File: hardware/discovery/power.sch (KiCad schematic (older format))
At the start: 9 parts, among them U2 MCP73831, U3 BD33IA5

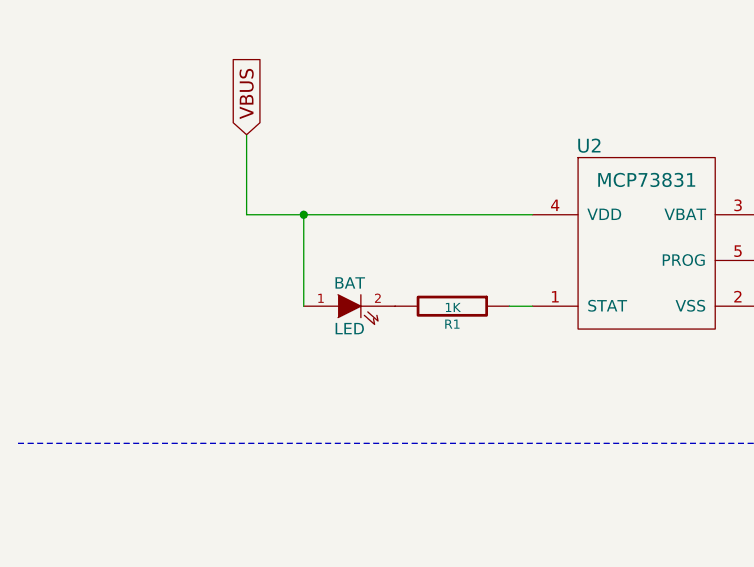
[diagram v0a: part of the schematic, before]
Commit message: Discovery: Fix channel button labels
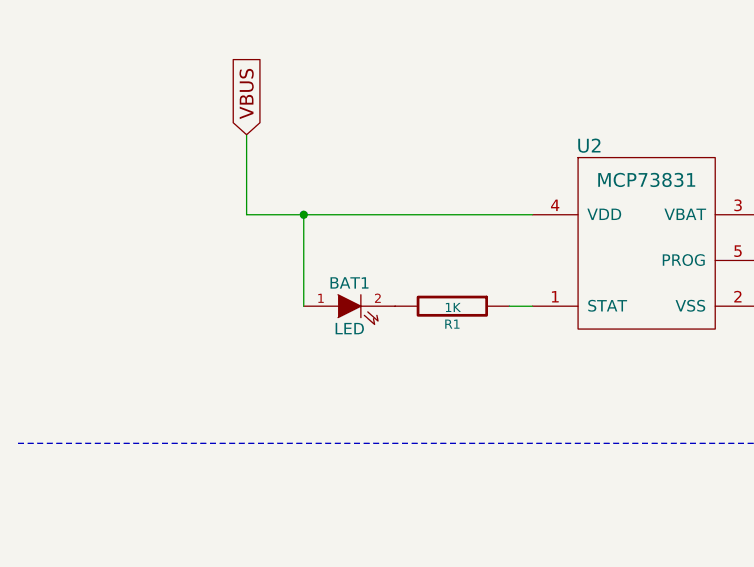
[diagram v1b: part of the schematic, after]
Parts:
- BAT1: renamed from BAT; footprint (none) -> Diodes_SMD:D_0805
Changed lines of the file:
@@
 $EndComp
 $Comp
-L GND #PWR02
+L GND #PWR07
 U 1 1 585D2F29
 P 4400 2900
-F 0 "#PWR02" H 4400 2900 30  0001 C CNN
+F 0 "#PWR07" H 4400 2900 30  0001 C CNN
 F 1 "GND" H 4400 2830 30  0001 C CNN
 F 2 "" H 4400 2900 60  0001 C CNN
@@
 	4700 2300 4700 1950
 $Comp
-L LED BAT
+L LED BAT1
 U 1 1 585D348C
 P 1950 2700
-F 0 "BAT" H 1950 2800 50  0000 C CNN
+F 0 "BAT1" H 1950 2800 50  0000 C CNN
 F 1 "LED" H 1950 2600 50  0000 C CNN
-F 2 "" H 1950 2700 60  0001 C CNN
+F 2 "Diodes_SMD:D_0805" H 1950 2700 60  0001 C CNN
 F 3 "" H 1950 2700 60  0000 C CNN
 	1    1950 2700
@@
 VBUS
 $Comp
-L PWR_FLAG #FLG03
+L PWR_FLAG #FLG08
 U 1 1 585D38B1
 P 4300 6300
-F 0 "#FLG03" H 4300 6395 30  0001 C CNN
+F 0 "#FLG08" H 4300 6395 30  0001 C CNN
 F 1 "PWR_FLAG" H 4300 6480 30  0000 C CNN
 F 2 "" H 4300 6300 60  0001 C CNN
@@
 $EndComp
 $Comp
-L PWR_FLAG #FLG04
+L PWR_FLAG #FLG09
 U 1 1 585D3922
 P 4300 6650
-F 0 "#FLG04" H 4300 6745 30  0001 C CNN
+F 0 "#FLG09" H 4300 6745 30  0001 C CNN
 F 1 "PWR_FLAG" H 4300 6830 30  0000 C CNN
 F 2 "" H 4300 6650 60  0001 C CNN
@@
 VIN
 $Comp
-L GND #PWR05
+L GND #PWR010
 U 1 1 585D49CE
 P 7750 2500
-F 0 "#PWR05" H 7750 2500 30  0001 C CNN
+F 0 "#PWR010" H 7750 2500 30  0001 C CNN
 F 1 "GND" H 7750 2430 30  0001 C CNN
 F 2 "" H 7750 2500 60  0001 C CNN
@@
 3V3
 $Comp
-L PWR_FLAG #FLG06
+L PWR_FLAG #FLG011
 U 1 1 585D561D
 P 4300 7000
-F 0 "#FLG06" H 4300 7095 30  0001 C CNN
+F 0 "#FLG011" H 4300 7095 30  0001 C CNN
 F 1 "PWR_FLAG" H 4300 7180 30  0000 C CNN
 F 2 "" H 4300 7000 60  0001 C CNN
@@
 $EndComp
 $Comp
-L GND #PWR07
+L GND #PWR012
 U 1 1 585D5C16
 P 9600 2300
-F 0 "#PWR07" H 9600 2300 30  0001 C CNN
+F 0 "#PWR012" H 9600 2300 30  0001 C CNN
 F 1 "GND" H 9600 2230 30  0001 C CNN
 F 2 "" H 9600 2300 60  0001 C CNN

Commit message: Discovery start power section
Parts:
- removed D27: DOUBLE_SCH_KCOM, TO_SOT_Packages_SMD:SOT-23_Handsoldering, symbol DOUBLE_SCH_KCOM
- added BT1: BATTERY, Connect:PINHEAD1-2, symbol BATTERY
- added CON1: USB-MICRO-B, Connect:USB_Micro-B, symbol USB-MICRO-B
- added D27: DOUBLE_SCH_KCOM_PMEG2005CT, TO_SOT_Packages_SMD:SOT-23, symbol DOUBLE_SCH_KCOM_PMEG2005CT
- C1, C2: footprint (none) -> Capacitors_SMD:C_0805
- C3: footprint (none) -> Capacitors_SMD:C_1206
- R1, R2: footprint (none) -> Resistors_SMD:R_0805
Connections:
- net labels added: FS_DM, FS_DP
- wire segments 19 -> 26
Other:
- note added: "R2 = 10K => 100mA charge\n"
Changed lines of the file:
@@
 LIBS:contrib
 LIBS:valves
-LIBS:w_connectors
 LIBS:stm32f4_disco_header
 LIBS:74xgxx
@@
 F 0 "R2" V 4130 2500 40  0000 C CNN
 F 1 "10K" V 4057 2501 40  0000 C CNN
-F 2 "" V 3980 2500 30  0001 C CNN
+F 2 "Resistors_SMD:R_0805" V 3980 2500 30  0001 C CNN
 F 3 "" H 4050 2500 30  0000 C CNN
 	1    4050 2500
@@
 F 0 "C1" H 4700 2600 40  0000 L CNN
 F 1 "10uF" H 4706 2415 40  0000 L CNN
-F 2 "" H 4738 2350 30  0001 C CNN
+F 2 "Capacitors_SMD:C_0805" H 4738 2350 30  0001 C CNN
 F 3 "" H 4700 2500 60  0000 C CNN
 	1    4700 2500
@@
 F 0 "R1" V 2480 2700 40  0000 C CNN
 F 1 "1K" V 2407 2701 40  0000 C CNN
-F 2 "" V 2330 2700 30  0001 C CNN
+F 2 "Resistors_SMD:R_0805" V 2330 2700 30  0001 C CNN
 F 3 "" H 2400 2700 30  0000 C CNN
 	1    2400 2700
@@
 	1    0    0    -1
 $EndComp
-$Comp
-L DOUBLE_SCH_KCOM D27
-U 1 1 585D4394
-P 5550 6750
-F 0 "D27" H 5700 6625 60  0000 C CNN
-F 1 "DOUBLE_SCH_KCOM" H 5550 6900 60  0000 C CNN
-F 2 "TO_SOT_Packages_SMD:SOT-23_Handsoldering" H 5550 6750 60  0001 C CNN
-F 3 "" H 5550 6750 60  0000 C CNN
-	1    5550 6750
-	-1   0    0    1
-$EndComp
-Text GLabel 5150 6750 0    60   Input ~ 0
+Text GLabel 5950 6750 2    60   Input ~ 0
 VBUS
 Text GLabel 5550 6550 1    60   Input ~ 0
 VIN
-Text GLabel 5950 6750 2    60   Input ~ 0
+Text GLabel 5150 6750 0    60   Input ~ 0
 VBAT
 Wire Wire Line
@@
 F 0 "C3" H 9600 2200 40  0000 L CNN
 F 1 "47uF" H 9606 2015 40  0000 L CNN
-F 2 "" H 9638 1950 30  0001 C CNN
+F 2 "Capacitors_SMD:C_1206" H 9638 1950 30  0001 C CNN
 F 3 "" H 9600 2100 60  0000 C CNN
 	1    9600 2100
@@
 F 0 "C2" H 7750 2200 40  0000 L CNN
 F 1 "4.7uF" H 7756 2015 40  0000 L CNN
-F 2 "" H 7788 1950 30  0001 C CNN
+F 2 "Capacitors_SMD:C_0805" H 7788 1950 30  0001 C CNN
 F 3 "" H 7750 2100 60  0000 C CNN
 	1    7750 2100
@@
 Wire Wire Line
 	3800 2500 3750 2500
+$Comp
+L USB-MICRO-B CON1
+U 1 1 585CF6A2
+P 4450 4500
+F 0 "CON1" H 4200 4950 60  0000 C CNN
+F 1 "USB-MICRO-B" H 4400 4000 60  0000 C CNN
+F 2 "Connect:USB_Micro-B" H 4450 4500 60  0001 C CNN
+F 3 "" H 4450 4500 60  0001 C CNN
+	1    4450 4500
+	1    0    0    -1
+$EndComp
+Wire Wire Line
+	5000 4200 5200 4200
+Wire Wire Line
+	5200 4200 5200 5000
+Wire Wire Line
+	5000 4350 5200 4350
+Connection ~ 5200 4350
+Wire Wire Line
+	5000 4650 5200 4650
+Connection ~ 5200 4650
+Wire Wire Line
+	5000 4800 5200 4800
+Connection ~ 5200 4800
+$Comp
+L GND #PWR013
+U 1 1 585CFC1E
+P 5200 5000
+F 0 "#PWR013" H 5200 5000 30  0001 C CNN
+F 1 "GND" H 5200 4930 30  0001 C CNN
+F 2 "" H 5200 5000 60  0001 C CNN
+F 3 "" H 5200 5000 60  0001 C CNN
+	1    5200 5000
+	1    0    0    -1
+$EndComp
+Text GLabel 3900 4200 0    60   Input ~ 0
+VBUS
+Wire Wire Line
+	3900 4800 3700 4800
+Wire Wire Line
+	3700 4800 3700 5000
+$Comp
+L GND #PWR014
+U 1 1 585CFC9F
+P 3700 5000
+F 0 "#PWR014" H 3700 5000 30  0001 C CNN
+F 1 "GND" H 3700 4930 30  0001 C CNN
+F 2 "" H 3700 5000 60  0001 C CNN
+F 3 "" H 3700 5000 60  0001 C CNN
+	1    3700 5000
+	1    0    0    -1
+$EndComp
+Text Notes 3800 3100 0    60   ~ 0
+R2 = 10K => 100mA charge\n
+$Comp
+L DOUBLE_SCH_KCOM_PMEG2005CT D27
+U 1 1 585D07BB
+P 5550 6750
+F 0 "D27" H 5700 6625 60  0000 C CNN
+F 1 "DOUBLE_SCH_KCOM_PMEG2005CT" H 5550 6900 60  0000 C CNN
+F 2 "TO_SOT_Packages_SMD:SOT-23" H 5550 6750 60  0001 C CNN
+F 3 "" H 5550 6750 60  0000 C CNN
+	1    5550 6750
+	-1   0    0    1
+$EndComp
+Text GLabel 3900 4350 0    60   Input ~ 0
+FS_DM
+Text GLabel 3900 4500 0    60   Input ~ 0
+FS_DP
+$Comp
+L BATTERY BT1
+U 1 1 585D1A2B
+P 2150 4500
+F 0 "BT1" H 2150 4700 50  0000 C CNN
+F 1 "BATTERY" H 2150 4310 50  0000 C CNN
+F 2 "Connect:PINHEAD1-2" H 2150 4500 60  0001 C CNN
+F 3 "" H 2150 4500 60  0000 C CNN
+	1    2150 4500
+	0    1    1    0
+$EndComp
+Text GLabel 2150 4200 1    60   Input ~ 0
+VBAT
+$Comp
+L GND #PWR015
+U 1 1 585D1BAC
+P 2150 4800
+F 0 "#PWR015" H 2150 4800 30  0001 C CNN
+F 1 "GND" H 2150 4730 30  0001 C CNN
+F 2 "" H 2150 4800 60  0001 C CNN
+F 3 "" H 2150 4800 60  0001 C CNN
+	1    2150 4800
+	1    0    0    -1
+$EndComp
 $EndSCHEMATC

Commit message: Discovery: Connect all button to the wakeup pin
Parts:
- BAT1: footprint Diodes_SMD:D_0805 -> LEDs:LED_0805
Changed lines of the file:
@@
 $EndComp
 $Comp
-L GND #PWR07
+L GND #PWR04
 U 1 1 585D2F29
 P 4400 2900
-F 0 "#PWR07" H 4400 2900 30  0001 C CNN
+F 0 "#PWR04" H 4400 2900 30  0001 C CNN
 F 1 "GND" H 4400 2830 30  0001 C CNN
 F 2 "" H 4400 2900 60  0001 C CNN
@@
 F 0 "BAT1" H 1950 2800 50  0000 C CNN
 F 1 "LED" H 1950 2600 50  0000 C CNN
-F 2 "Diodes_SMD:D_0805" H 1950 2700 60  0001 C CNN
+F 2 "LEDs:LED_0805" H 1950 2700 60  0001 C CNN
 F 3 "" H 1950 2700 60  0000 C CNN
 	1    1950 2700
@@
 VBUS
 $Comp
-L PWR_FLAG #FLG08
+L PWR_FLAG #FLG05
 U 1 1 585D38B1
 P 4300 6300
-F 0 "#FLG08" H 4300 6395 30  0001 C CNN
+F 0 "#FLG05" H 4300 6395 30  0001 C CNN
 F 1 "PWR_FLAG" H 4300 6480 30  0000 C CNN
 F 2 "" H 4300 6300 60  0001 C CNN
@@
 $EndComp
 $Comp
-L PWR_FLAG #FLG09
+L PWR_FLAG #FLG06
 U 1 1 585D3922
 P 4300 6650
-F 0 "#FLG09" H 4300 6745 30  0001 C CNN
+F 0 "#FLG06" H 4300 6745 30  0001 C CNN
 F 1 "PWR_FLAG" H 4300 6830 30  0000 C CNN
 F 2 "" H 4300 6650 60  0001 C CNN
@@
 VIN
 $Comp
-L GND #PWR010
+L GND #PWR07
 U 1 1 585D49CE
 P 7750 2500
-F 0 "#PWR010" H 7750 2500 30  0001 C CNN
+F 0 "#PWR07" H 7750 2500 30  0001 C CNN
 F 1 "GND" H 7750 2430 30  0001 C CNN
 F 2 "" H 7750 2500 60  0001 C CNN
@@
 3V3
 $Comp
-L PWR_FLAG #FLG011
+L PWR_FLAG #FLG08
 U 1 1 585D561D
 P 4300 7000
-F 0 "#FLG011" H 4300 7095 30  0001 C CNN
+F 0 "#FLG08" H 4300 7095 30  0001 C CNN
 F 1 "PWR_FLAG" H 4300 7180 30  0000 C CNN
 F 2 "" H 4300 7000 60  0001 C CNN
@@
 $EndComp
 $Comp
-L GND #PWR012
+L GND #PWR09
 U 1 1 585D5C16
 P 9600 2300
-F 0 "#PWR012" H 9600 2300 30  0001 C CNN
+F 0 "#PWR09" H 9600 2300 30  0001 C CNN
 F 1 "GND" H 9600 2230 30  0001 C CNN
 F 2 "" H 9600 2300 60  0001 C CNN
@@
 Connection ~ 5200 4800
 $Comp
-L GND #PWR013
+L GND #PWR010
 U 1 1 585CFC1E
 P 5200 5000
-F 0 "#PWR013" H 5200 5000 30  0001 C CNN
+F 0 "#PWR010" H 5200 5000 30  0001 C CNN
 F 1 "GND" H 5200 4930 30  0001 C CNN
 F 2 "" H 5200 5000 60  0001 C CNN
@@
 	3700 4800 3700 5000
 $Comp
-L GND #PWR014
+L GND #PWR011
 U 1 1 585CFC9F
 P 3700 5000
-F 0 "#PWR014" H 3700 5000 30  0001 C CNN
+F 0 "#PWR011" H 3700 5000 30  0001 C CNN
 F 1 "GND" H 3700 4930 30  0001 C CNN
 F 2 "" H 3700 5000 60  0001 C CNN
@@
 VBAT
 $Comp
-L GND #PWR015
+L GND #PWR012
 U 1 1 585D1BAC
 P 2150 4800
-F 0 "#PWR015" H 2150 4800 30  0001 C CNN
+F 0 "#PWR012" H 2150 4800 30  0001 C CNN
 F 1 "GND" H 2150 4730 30  0001 C CNN
 F 2 "" H 2150 4800 60  0001 C CNN

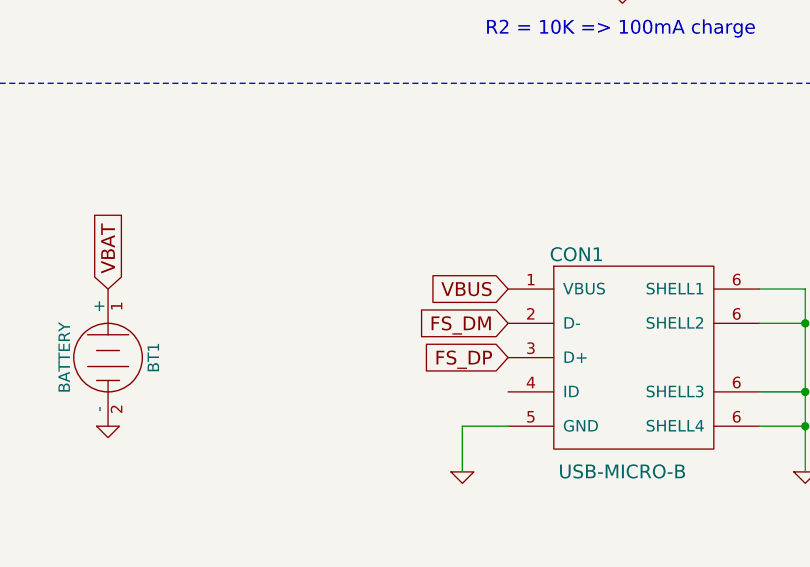
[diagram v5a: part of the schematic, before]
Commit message: Discovery: STM32F4 power a filtering
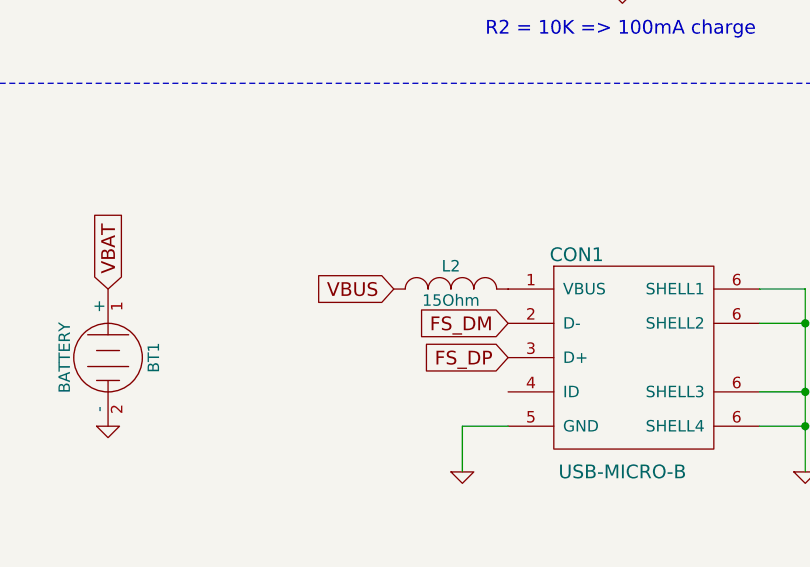
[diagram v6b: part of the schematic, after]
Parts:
- added L2: 15Ohm, symbol INDUCTOR_SMALL
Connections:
- net VBUS: now also L2.1; no longer CON1.1 (VBUS)
- new net: CON1.1 (VBUS), L2.2
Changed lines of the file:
@@
 $EndComp
 $Comp
-L GND #PWR04
+L GND #PWR02
 U 1 1 585D2F29
 P 4400 2900
-F 0 "#PWR04" H 4400 2900 30  0001 C CNN
+F 0 "#PWR02" H 4400 2900 30  0001 C CNN
 F 1 "GND" H 4400 2830 30  0001 C CNN
 F 2 "" H 4400 2900 60  0001 C CNN
@@
 VBUS
 $Comp
-L PWR_FLAG #FLG05
+L PWR_FLAG #FLG03
 U 1 1 585D38B1
 P 4300 6300
-F 0 "#FLG05" H 4300 6395 30  0001 C CNN
+F 0 "#FLG03" H 4300 6395 30  0001 C CNN
 F 1 "PWR_FLAG" H 4300 6480 30  0000 C CNN
 F 2 "" H 4300 6300 60  0001 C CNN
@@
 $EndComp
 $Comp
-L PWR_FLAG #FLG06
+L PWR_FLAG #FLG04
 U 1 1 585D3922
 P 4300 6650
-F 0 "#FLG06" H 4300 6745 30  0001 C CNN
+F 0 "#FLG04" H 4300 6745 30  0001 C CNN
 F 1 "PWR_FLAG" H 4300 6830 30  0000 C CNN
 F 2 "" H 4300 6650 60  0001 C CNN
@@
 VIN
 $Comp
-L GND #PWR07
+L GND #PWR05
 U 1 1 585D49CE
 P 7750 2500
-F 0 "#PWR07" H 7750 2500 30  0001 C CNN
+F 0 "#PWR05" H 7750 2500 30  0001 C CNN
 F 1 "GND" H 7750 2430 30  0001 C CNN
 F 2 "" H 7750 2500 60  0001 C CNN
@@
 3V3
 $Comp
-L PWR_FLAG #FLG08
+L PWR_FLAG #FLG06
 U 1 1 585D561D
 P 4300 7000
-F 0 "#FLG08" H 4300 7095 30  0001 C CNN
+F 0 "#FLG06" H 4300 7095 30  0001 C CNN
 F 1 "PWR_FLAG" H 4300 7180 30  0000 C CNN
 F 2 "" H 4300 7000 60  0001 C CNN
@@
 $EndComp
 $Comp
-L GND #PWR09
+L GND #PWR07
 U 1 1 585D5C16
 P 9600 2300
-F 0 "#PWR09" H 9600 2300 30  0001 C CNN
+F 0 "#PWR07" H 9600 2300 30  0001 C CNN
 F 1 "GND" H 9600 2230 30  0001 C CNN
 F 2 "" H 9600 2300 60  0001 C CNN
@@
 Connection ~ 5200 4800
 $Comp
-L GND #PWR010
+L GND #PWR08
 U 1 1 585CFC1E
 P 5200 5000
-F 0 "#PWR010" H 5200 5000 30  0001 C CNN
+F 0 "#PWR08" H 5200 5000 30  0001 C CNN
 F 1 "GND" H 5200 4930 30  0001 C CNN
 F 2 "" H 5200 5000 60  0001 C CNN
@@
 	1    0    0    -1
 $EndComp
-Text GLabel 3900 4200 0    60   Input ~ 0
+Text GLabel 3400 4200 0    60   Input ~ 0
 VBUS
 Wire Wire Line
@@
 	3700 4800 3700 5000
 $Comp
-L GND #PWR011
+L GND #PWR09
 U 1 1 585CFC9F
 P 3700 5000
-F 0 "#PWR011" H 3700 5000 30  0001 C CNN
+F 0 "#PWR09" H 3700 5000 30  0001 C CNN
 F 1 "GND" H 3700 4930 30  0001 C CNN
 F 2 "" H 3700 5000 60  0001 C CNN
@@
 VBAT
 $Comp
-L GND #PWR012
+L GND #PWR010
 U 1 1 585D1BAC
 P 2150 4800
-F 0 "#PWR012" H 2150 4800 30  0001 C CNN
+F 0 "#PWR010" H 2150 4800 30  0001 C CNN
 F 1 "GND" H 2150 4730 30  0001 C CNN
 F 2 "" H 2150 4800 60  0001 C CNN
@@
 	1    0    0    -1
 $EndComp
+$Comp
+L INDUCTOR_SMALL L2
+U 1 1 58628564
+P 3650 4200
+F 0 "L2" H 3650 4300 50  0000 C CNN
+F 1 "15Ohm" H 3650 4150 50  0000 C CNN
+F 2 "" H 3650 4200 60  0000 C CNN
+F 3 "" H 3650 4200 60  0000 C CNN
+	1    3650 4200
+	1    0    0    -1
+$EndComp

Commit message: Discovery: Add micro SD card
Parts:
- L2: footprint (none) -> Capacitors_SMD:C_0805
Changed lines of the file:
@@
 F 0 "L2" H 3650 4300 50  0000 C CNN
 F 1 "15Ohm" H 3650 4150 50  0000 C CNN
-F 2 "" H 3650 4200 60  0001 C CNN
+F 2 "Capacitors_SMD:C_0805" H 3650 4200 60  0001 C CNN
 F 3 "" H 3650 4200 60  0000 C CNN
 	1    3650 4200
